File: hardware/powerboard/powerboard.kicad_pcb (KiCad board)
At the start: 4 copper layers, 81.2 x 50.7 mm, 73 parts, among them J1 USB_B_Micro, J10 5V, J11 3V3, J2 Boot, J3 Keysboard Header, J4 Display, J5 Debug, J7 UART_0, J8 I2C_0, J9 I2C_1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

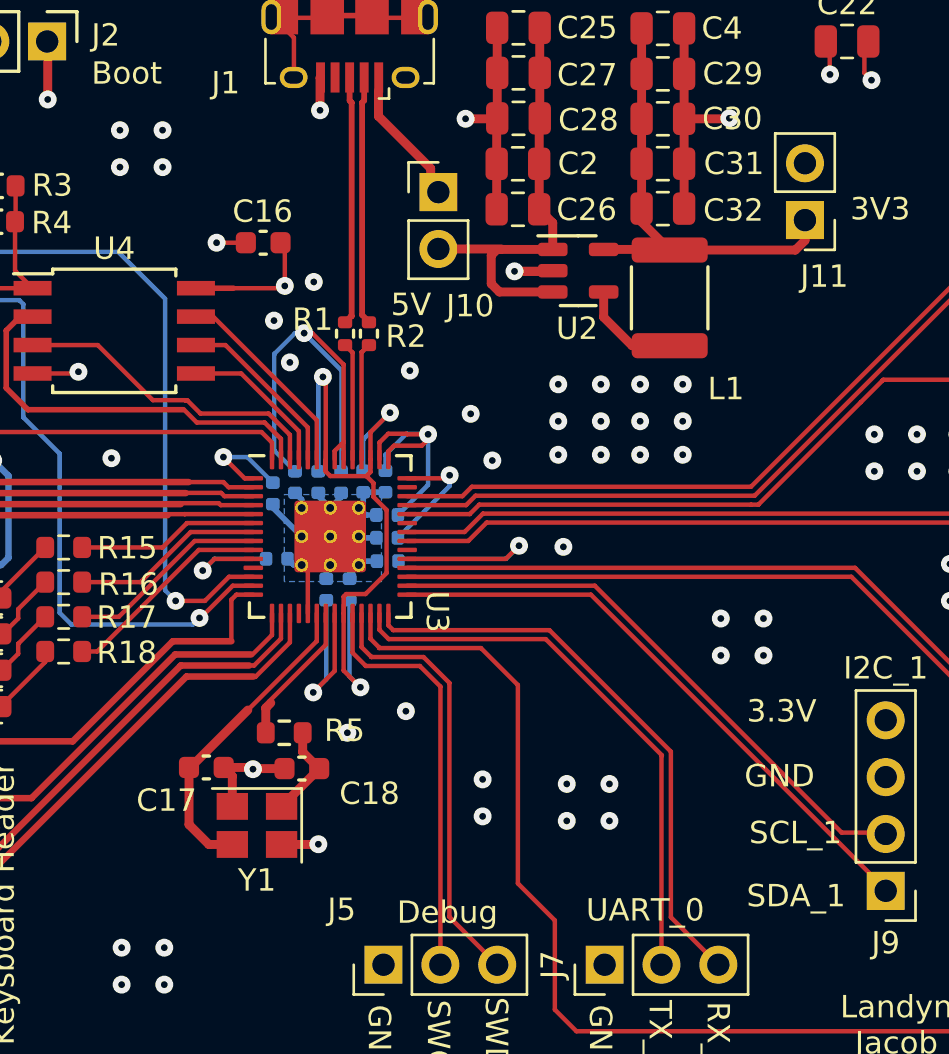
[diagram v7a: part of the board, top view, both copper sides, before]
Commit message: GND Vias and RP2040 Footprint change
When JLC was acting weird, I changed the footprint of the RP2040 to the generic version without thermal vias. I now want the thermal vias again, as they provide an easy GND connection for the chip.
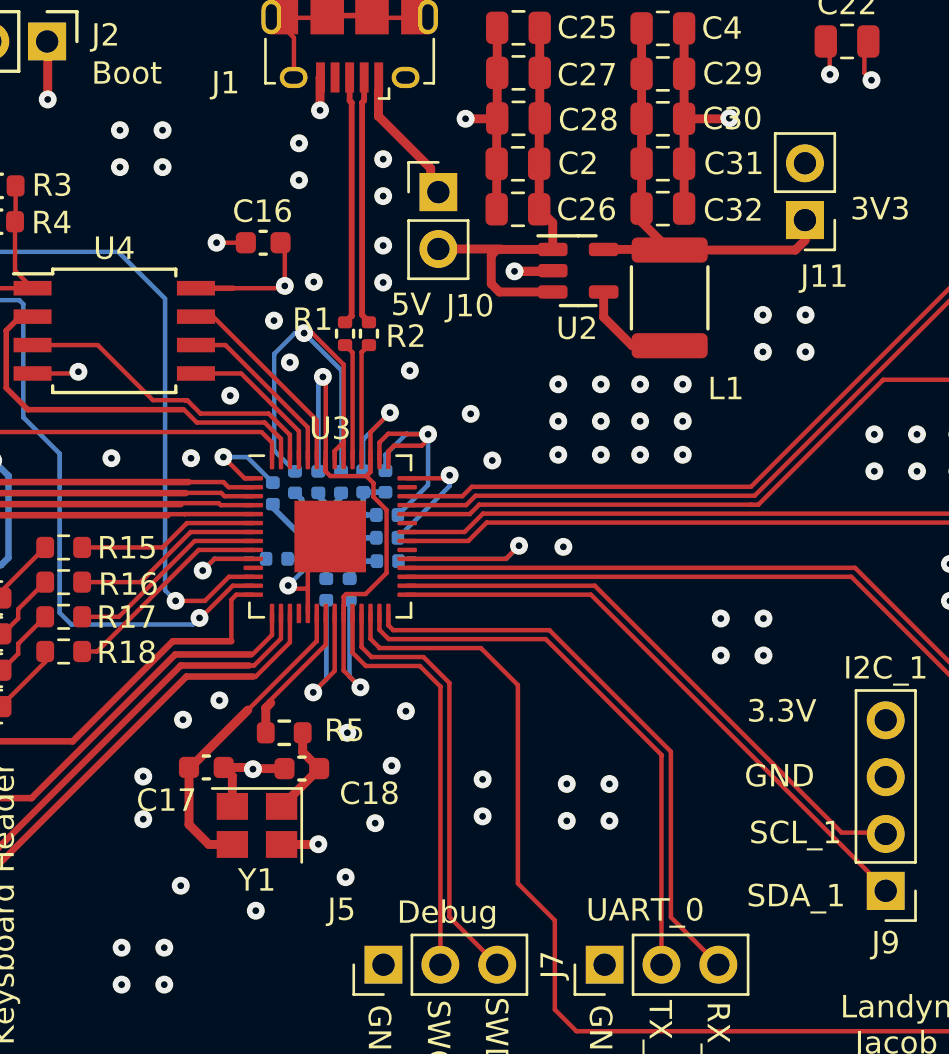
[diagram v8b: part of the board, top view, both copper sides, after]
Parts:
- U3: footprint RP2040_minimal:RP2040-QFN-56 -> Package_DFN_QFN:QFN-56-1EP_7x7mm_P0.4mm_EP3.2x3.2mm
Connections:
- net Net-(C2-Pad1) renamed +5V
- net Net-(J1-Pad1) renamed VBUS
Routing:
- net GND: track 94.1 -> 97.9 mm, vias 105 -> 127
